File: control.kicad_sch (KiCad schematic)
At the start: 50 parts, among them IC10 INA260AIPWR, IC15 SN65HVD1782QDRQ1, IC16 TPS2121RUXR, IC17 TCAN1046AVDRQ1, IC21 MCP2517FD-H_SL, U2 RP2354A_60QFN, Y1 ABM8AIG-20MHz-12-2Z-T3, Y2 ABM8-272-T3

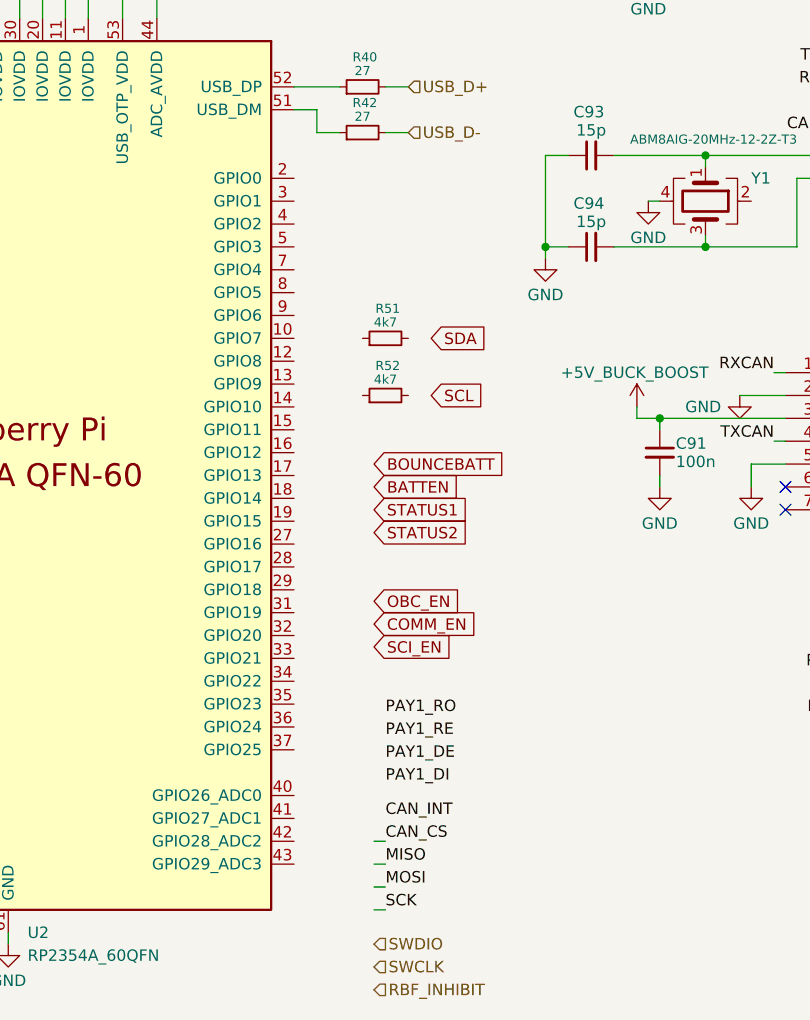
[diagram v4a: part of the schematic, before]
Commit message: updated the schematic to remove connection to rocksat, linked schmatic symbols to footprints
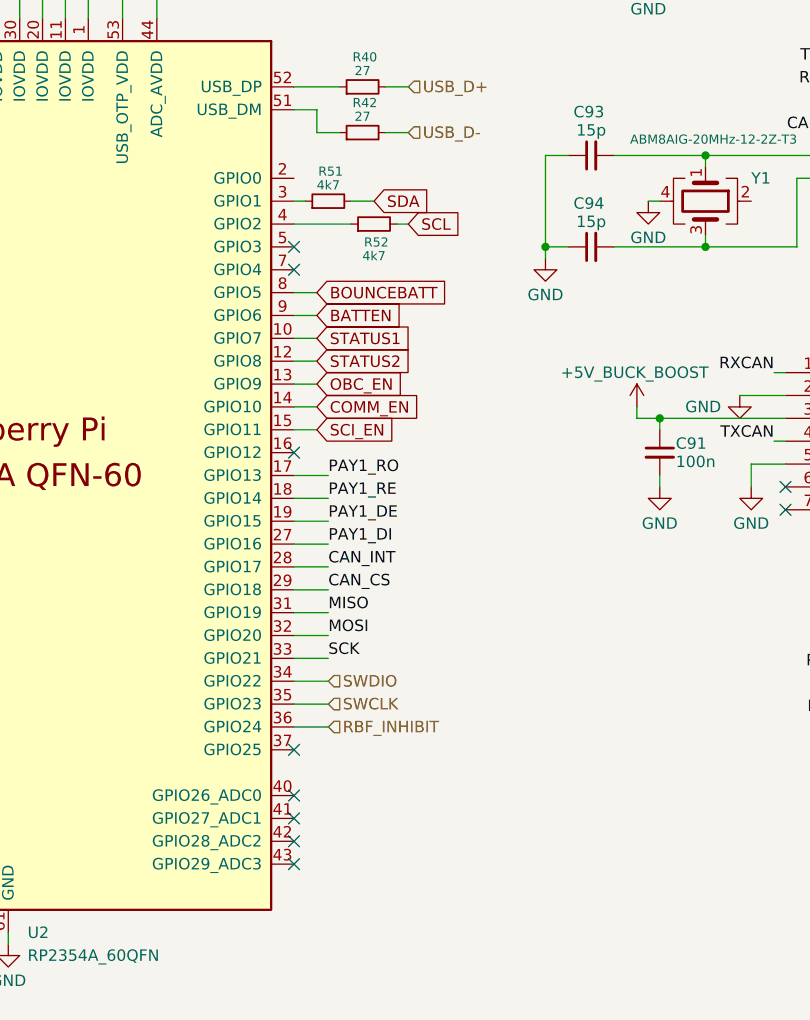
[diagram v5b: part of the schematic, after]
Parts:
- C13, C58, C59, C60, C61, C62, C63, C64, C66, C67, C68, C69, C75, C89, C90, C91, C92, C93, C94: footprint (none) -> Capacitor_SMD:C_0402_1005Metric
- C65, C70, C71, C72, C73, C74: footprint (none) -> Capacitor_SMD:C_0603_1608Metric
- D14: footprint DIOM5225X250N -> HEDGE2:CDBA240LL-HF
- IC10: footprint SOP65P640X120-16N -> HEDGE2:INA260AIPWR
- IC15: footprint SOIC127P600X175-8N -> HEDGE2:SN65HVD1782QDRQ1
- IC16: footprint TPS2121RUXR -> HEDGE2:TPS2121RUXR
- IC17: footprint SOIC127P600X175-14N -> HEDGE2:TCAN1046AVDRQ1
- IC21: footprint SOIC127P600X175-14N -> HEDGE2:MCP2517FD-H_SL
- L1: footprint AOTAB201610S3R3101T -> HEDGE2:AOTAB201610S3R3101T
- PS1: footprint SOT95P280X145-5N -> HEDGE2:TLV75733PDBVR
- R40, R42, R44, R45, R46, R47, R48, R49, R50, R51, R52, R53, R54, R69: footprint (none) -> Resistor_SMD:R_0402_1005Metric
- U2: footprint RP2354A_60QFN_minimal:RP2350-QFN-60-1EP_7x7_P0.4mm_EP3.4x3.4mm_ThermalVias -> HEDGE2:RP2354A
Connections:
- net BATTEN: now also U2.9 (GPIO6)
- net BOUNCEBATT: now also U2.8 (GPIO5)
- net CAN_CS: now also U2.29 (GPIO18)
- net CAN_INT: now also U2.28 (GPIO17)
- net COMM_EN: now also U2.14 (GPIO10)
- net MISO: now also U2.31 (GPIO19)
- net MOSI: now also U2.32 (GPIO20)
- net OBC_EN: now also U2.13 (GPIO9)
- net PAY1_DE: now also U2.19 (GPIO15)
- net PAY1_DI: now also U2.27 (GPIO16)
- net PAY1_RE: now also U2.18 (GPIO14)
- net PAY1_RO: now also U2.17 (GPIO13)
- net RBF_INHIBIT: now also U2.36 (GPIO24)
- net SCI_EN: now also U2.15 (GPIO11)
- net SCK: now also U2.33 (GPIO21)
- net SCL: now also R52.2
- net SDA: now also R51.2
- net STATUS1: now also U2.10 (GPIO7)
- net STATUS2: now also U2.12 (GPIO8)
- net SWCLK: now also U2.35 (GPIO23)
- net SWDIO: now also U2.34 (GPIO22)
- net at U2.3 (GPIO1): now also R51.1
- net at U2.4 (GPIO2): now also R52.1
- no-connect marks 18 -> 26
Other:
- moved on the sheet: R51, R52

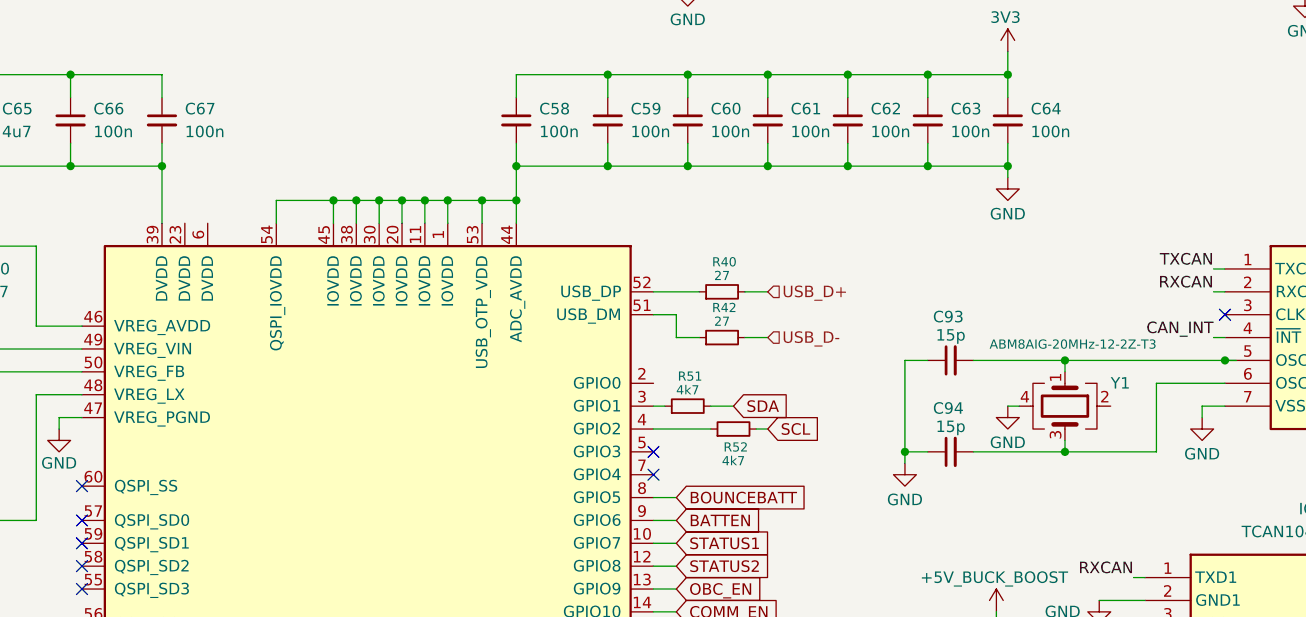
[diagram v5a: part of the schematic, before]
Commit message: Added most 3d models, continued layout
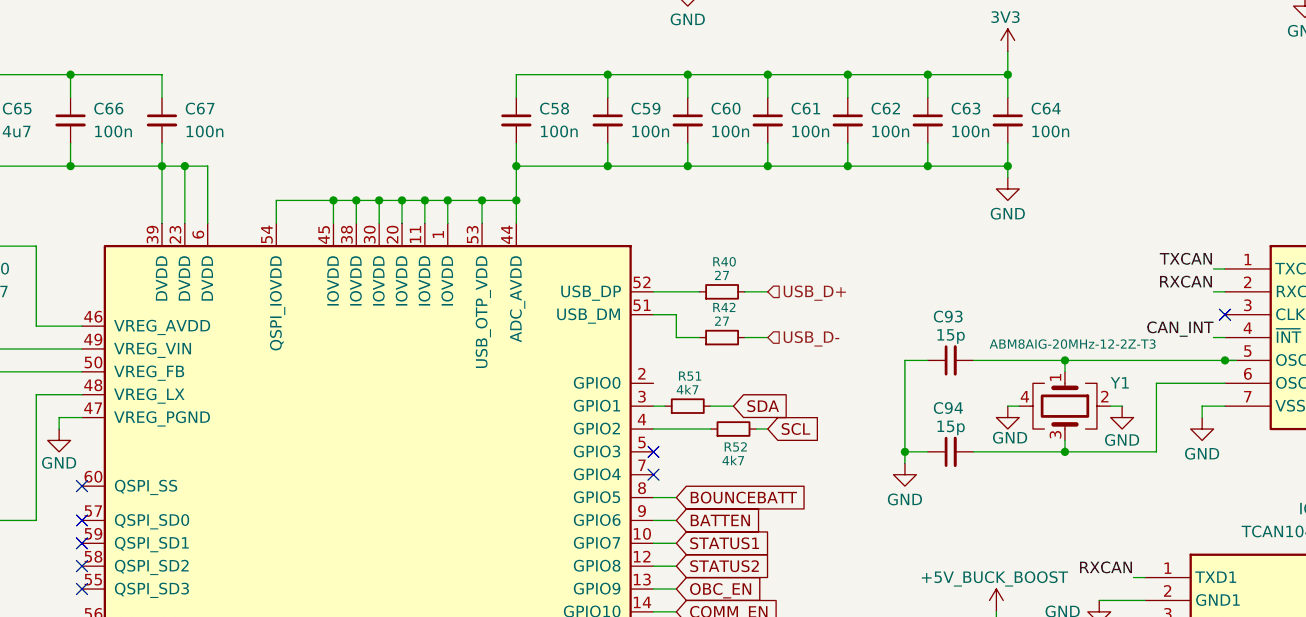
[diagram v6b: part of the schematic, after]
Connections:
- net GND: now also U2.23 (DVDD), U2.6 (DVDD), Y1.2
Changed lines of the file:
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@@
 	)
 	(junction
+		(at 96.52 67.31)
+		(diameter 0)
+		(color 0 0 0 0)
+	)
+	(junction
 		(at 71.12 29.21)
 		(diameter 0)
@@
 	(wire
 		(pts
+			(xy 93.98 67.31) (xy 96.52 67.31)
+		)
+		(stroke
+			(width 0)
+			(type default)
+		)
+	)
+	(wire
+		(pts
 			(xy 213.36 146.05) (xy 214.63 146.05)
 		)
@@
 	(wire
 		(pts
+			(xy 99.06 73.66) (xy 99.06 67.31)
+		)
+		(stroke
+			(width 0)
+			(type default)
+		)
+	)
+	(wire
+		(pts
 			(xy 73.66 59.69) (xy 73.66 57.15)
 		)
@@
 	(wire
 		(pts
+			(xy 99.06 67.31) (xy 96.52 67.31)
+		)
+		(stroke
+			(width 0)
+			(type default)
+		)
+	)
+	(wire
+		(pts
 			(xy 148.59 124.46) (xy 152.4 124.46)
 		)
@@
 	(wire
 		(pts
+			(xy 96.52 67.31) (xy 96.52 73.66)
+		)
+		(stroke
+			(width 0)
+			(type default)
+		)
+	)
+	(wire
+		(pts
 			(xy 48.26 137.16) (xy 50.8 137.16)
 		)
@@
 	(wire
 		(pts
+			(xy 199.39 93.98) (xy 200.66 93.98)
+		)
+		(stroke
+			(width 0)
+			(type default)
+		)
+	)
+	(wire
+		(pts
 			(xy 73.66 144.78) (xy 76.2 144.78)
 		)
@@
 		)
 		(property "Value" "GND"
-			(at 187.96 98.044 0)
+			(at 188.214 97.536 0)
 			(effects
 				(font
@@
 					(unit 1)
 				)
+			)
+		)
+	)
+	(symbol
+		(lib_id "power:GND")
+		(at 200.66 93.98 0)
+		(unit 1)
+		(exclude_from_sim no)
+		(in_bom yes)
+		(on_board yes)
+		(dnp no)
+		(property "Reference" "#PWR010"
+			(at 200.66 100.33 0)
+			(effects
+				(font
+					(size 1.27 1.27)
+				)
+				(hide yes)
+			)
+		)
+		(property "Value" "GND"
+			(at 200.66 97.79 0)
+			(effects
+				(font
+					(size 1.27 1.27)
+				)
+			)
+		)
+		(property "Footprint" ""
+			(at 200.66 93.98 0)
+			(effects
+				(font
+					(size 1.27 1.27)
+				)
+				(hide yes)
+			)
+		)
+		(property "Datasheet" ""
+			(at 200.66 93.98 0)
+			(effects
+				(font
+					(size 1.27 1.27)
+				)
+				(hide yes)
+			)
+		)
+		(property "Description" "Power symbol creates a global label with name \"GND\" , ground"
+			(at 200.66 93.98 0)
+			(effects
+				(font
+					(size 1.27 1.27)
+				)
+				(hide yes)
+			)
+		)
+		(pin "1"
+		)
+		(instances
+			(project "EPS"
+				(path "/7b605902-d0e0-4baa-b797-611cfe27637f/8396a4b2-0cce-4978-8662-437d163a7808"
+					(reference "#PWR010")
+					(unit 1)
+				)

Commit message: Initial layout completed
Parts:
- added C1: 100n, Capacitor_SMD:C_0402_1005Metric, symbol Device:C_Small
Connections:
- net 1V1: now also U2.23 (DVDD), U2.39 (DVDD), U2.6 (DVDD)
- net 3V3: now also U2.1 (IOVDD), U2.11 (IOVDD), U2.20 (IOVDD), U2.30 (IOVDD), U2.38 (IOVDD), U2.44 (ADC_AVDD), U2.45 (IOVDD), U2.53 (USB_OTP_VDD), U2.54 (QSPI_IOVDD), C1.1
- net GND: now also C1.2; no longer U2.1 (IOVDD), U2.11 (IOVDD), U2.20 (IOVDD), U2.23 (DVDD), U2.30 (IOVDD), U2.38 (IOVDD), U2.39 (DVDD), U2.44 (ADC_AVDD), U2.45 (IOVDD), U2.53 (USB_OTP_VDD), U2.54 (QSPI_IOVDD), U2.6 (DVDD)
- net at C93.2, Y1.1: no longer IC21.5 (OSC2)
- no-connect marks 26 -> 27
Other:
- moved on the sheet: C58, C59, C60, C61, C62, C63, C64, C65, C66, C67
